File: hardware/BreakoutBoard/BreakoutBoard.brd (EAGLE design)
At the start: 90 x 56 mm, 38 parts, among them J1 CON-71741-2184-TOP, J10 CON-2X3-RASTER, J11 CON-2X3-RASTER, J12 CON-2X3-RASTER, J13 CON-2X4-RASTER, J2 CON-71741-2184-BOT, J3 CON-2X4-RASTER, J4 CON-2X10-RASTER, J5 CON-2X3-RASTER, J6 CON-2X3-RASTER, J7 CON-2X3-RASTER, J8 CON-2X3-RASTER, J9 CON-2X3-RASTER, M1 MOUNT-HOLE3.3, M2 MOUNT-HOLE3.3, M3 MOUNT-HOLE3.3, M4 MOUNT-HOLE3.3, M5 FIDUCIAL1X2, M6 FIDUCIAL1X2, M7 FIDUCIAL1X2, M8 FIDUCIAL1X2

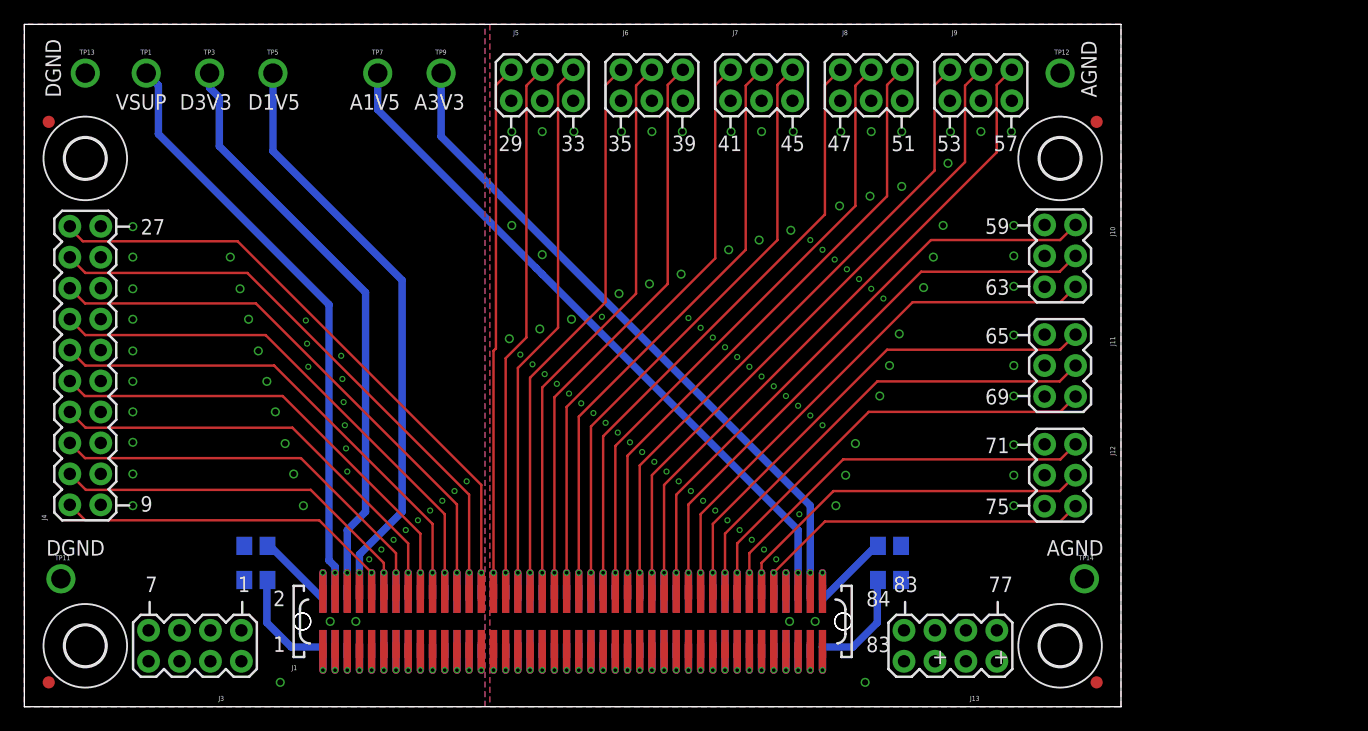
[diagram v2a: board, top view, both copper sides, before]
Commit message: - Ground planes changed - Supply wires
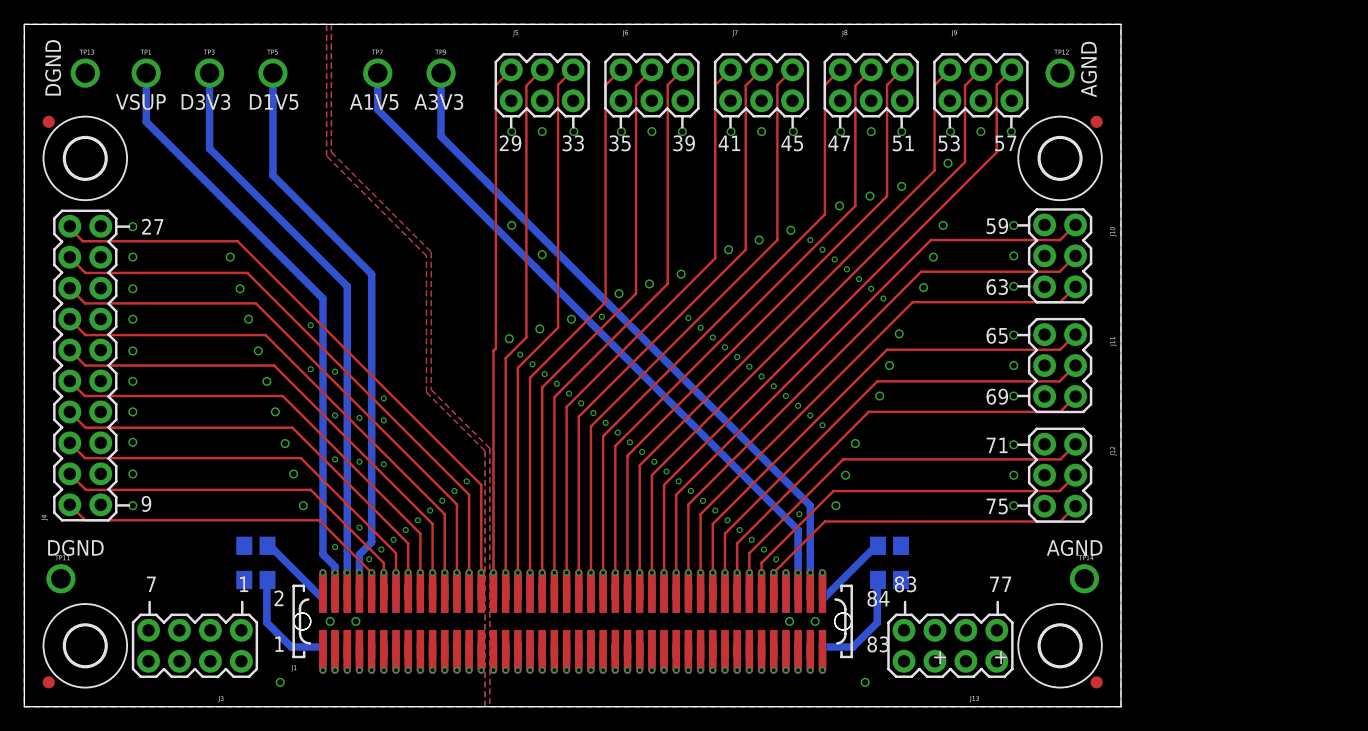
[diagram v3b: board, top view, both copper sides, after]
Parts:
- moved LOGO4 46.6 mm to (68.0, 15.0)
- moved LOGO1 45.9 mm to (12.0, 15.0)
- moved LOGO3 43.6 mm to (68.0, 25.5)
- moved LOGO2 32.9 mm to (12.0, 25.5)
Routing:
- net 8: track 76.5 -> 74.4 mm
- net 6: track 72.4 -> 71.2 mm
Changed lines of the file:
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@@
 <setting verticaltext="up"/>
 </settings>
-<grid distance="1" unitdist="mm" unit="mm" style="dots" multiple="1" display="yes" altdistance="0.1" altunitdist="mm" altunit="mm"/>
+<grid distance="1" unitdist="mm" unit="mm" style="dots" multiple="1" display="yes" altdistance="0.5" altunitdist="mm" altunit="mm"/>
 <layers>
-<layer number="1" name="Top" color="4" fill="1" visible="no" active="yes"/>
+<layer number="1" name="Top" color="4" fill="1" visible="yes" active="yes"/>
 <layer number="2" name="Even" color="2" fill="1" visible="no" active="yes"/>
-<layer number="3" name="Odd" color="4" fill="1" visible="yes" active="yes"/>
+<layer number="3" name="Odd" color="4" fill="1" visible="no" active="yes"/>
 <layer number="14" name="Route14" color="1" fill="6" visible="no" active="no"/>
 <layer number="15" name="Route15" color="4" fill="6" visible="no" active="no"/>
-<layer number="16" name="Bottom" color="1" fill="1" visible="yes" active="yes"/>
+<layer number="16" name="Bottom" color="1" fill="1" visible="no" active="yes"/>
 <layer number="17" name="Pads" color="2" fill="1" visible="yes" active="yes"/>
 <layer number="18" name="Vias" color="2" fill="1" visible="yes" active="yes"/>
@@
 <element name="M7" library="powerboard" package="FIDUCIAL-1X2" value="FIDUCIAL1X2" x="88" y="48"/>
 <element name="M8" library="powerboard" package="FIDUCIAL-1X2" value="FIDUCIAL1X2" x="88" y="2"/>
-<element name="LOGO1" library="Logo" package="LOGO-ISIS-10MM-GOLD" value="LOGO-ISIS-600MIL-10MM-AU" x="28" y="58"/>
-<element name="LOGO2" library="Logo" package="LOGO-VANDERBILT-10MM-GOLD" value="LOGO-VANDERBILT-600MIL-10MM-AU" x="17" y="58"/>
-<element name="LOGO3" library="Logo" package="LOGO-MARMOTE-10MM-GOLD" value="LOGO-MARMOTE-600MIL-10MM-AU" x="39" y="58"/>
-<element name="LOGO4" library="Logo" package="LOGO-MAGNIFYING-GLASS-10MM-GOLD" value="LOGO-MAGNIFYING-GLASS-600MIL-10MM-AU" x="50" y="58"/>
+<element name="LOGO1" library="Logo" package="LOGO-ISIS-10MM-GOLD" value="LOGO-ISIS-600MIL-10MM-AU" x="12" y="15"/>
+<element name="LOGO2" library="Logo" package="LOGO-VANDERBILT-10MM-GOLD" value="LOGO-VANDERBILT-600MIL-10MM-AU" x="12" y="25.5"/>
+<element name="LOGO3" library="Logo" package="LOGO-MARMOTE-10MM-GOLD" value="LOGO-MARMOTE-600MIL-10MM-AU" x="68" y="25.5"/>
+<element name="LOGO4" library="Logo" package="LOGO-MAGNIFYING-GLASS-10MM-GOLD" value="LOGO-MAGNIFYING-GLASS-600MIL-10MM-AU" x="68" y="15"/>
 <element name="TP1" library="BreakoutBoard" package="TESTPOINT" value="TESTPOINT-BLUE" x="10" y="52">
 <attribute name="DIGI-KEY#" value="5122K-ND" x="10" y="52" size="1.778" layer="27" display="off"/>
@@
 <vertex x="0" y="0"/>
 <vertex x="37.8" y="0"/>
-<vertex x="37.8" y="56"/>
+<vertex x="37.8" y="21"/>
+<vertex x="33" y="25.8"/>
+<vertex x="33" y="37"/>
+<vertex x="24.8" y="45.2"/>
+<vertex x="24.8" y="56"/>
 </polygon>
 <polygon width="0.2032" layer="16">
@@
 <vertex x="0" y="0"/>
 <vertex x="37.8" y="0"/>
-<vertex x="37.8" y="56"/>
+<vertex x="37.8" y="21"/>
+<vertex x="33" y="25.8"/>
+<vertex x="33" y="37"/>
+<vertex x="24.8" y="45.2"/>
+<vertex x="24.8" y="56"/>
 </polygon>
 <polygon width="0.2032" layer="3">
@@
 <vertex x="0" y="0"/>
 <vertex x="37.8" y="0"/>
-<vertex x="37.8" y="56"/>
+<vertex x="37.8" y="21"/>
+<vertex x="33" y="25.8"/>
+<vertex x="33" y="37"/>
+<vertex x="24.8" y="45.2"/>
+<vertex x="24.8" y="56"/>
 </polygon>
 <polygon width="0.2032" layer="2">
@@
 <vertex x="0" y="0"/>
 <vertex x="37.8" y="0"/>
-<vertex x="37.8" y="56"/>
+<vertex x="37.8" y="21"/>
+<vertex x="33" y="25.8"/>
+<vertex x="33" y="37"/>
+<vertex x="24.8" y="45.2"/>
+<vertex x="24.8" y="56"/>
 </polygon>
 <via x="8.9" y="16.5" extent="1-16" drill="0.5"/>
@@
 <via x="34.3" y="16.9" extent="1-16" drill="0.3048"/>
 <via x="35.3" y="17.7" extent="1-16" drill="0.3048"/>
-<via x="26.5" y="19.3" extent="1-16" drill="0.3048"/>
-<via x="26.4" y="21.2" extent="1-16" drill="0.3048"/>
-<via x="26.3" y="23.1" extent="1-16" drill="0.3048"/>
-<via x="26.2" y="25" extent="1-16" drill="0.3048"/>
-<via x="26.1" y="26.9" extent="1-16" drill="0.3048"/>
-<via x="26" y="28.8" extent="1-16" drill="0.3048"/>
-<via x="23.3" y="27.9" extent="1-16" drill="0.3048"/>
-<via x="23.2" y="29.8" extent="1-16" drill="0.3048"/>
-<via x="23.1" y="31.7" extent="1-16" drill="0.3048"/>
+<via x="27.5" y="20.1" extent="1-16" drill="0.3048"/>
+<via x="29.5" y="19.9" extent="1-16" drill="0.3048"/>
+<via x="25.5" y="23.9" extent="1-16" drill="0.3048"/>
+<via x="27.5" y="23.7" extent="1-16" drill="0.3048"/>
+<via x="29.5" y="23.5" extent="1-16" drill="0.3048"/>
+<via x="29.5" y="25.3" extent="1-16" drill="0.3048"/>
+<via x="23.5" y="27.7" extent="1-16" drill="0.3048"/>
+<via x="25.5" y="27.5" extent="1-16" drill="0.3048"/>
+<via x="23.5" y="31.3" extent="1-16" drill="0.3048"/>
 <via x="36.3" y="18.5" extent="1-16" drill="0.3048"/>
+<via x="25.5" y="20.3" extent="1-16" drill="0.3048"/>
+<via x="25.5" y="13.1" extent="1-16" drill="0.3048"/>
+<via x="27.5" y="14.7" extent="1-16" drill="0.3048"/>
 </signal>
 <signal name="1">
@@
 <wire x1="16.5" y1="2.5" x2="18.3" y2="2.5" width="0.2032" layer="2"/>
 <wire x1="19" y1="3.2" x2="18.3" y2="2.5" width="0.2032" layer="2"/>
-<wire x1="10" y1="52" x2="11" y2="51" width="0.6096" layer="16"/>
-<wire x1="11" y1="51" x2="11" y2="47" width="0.6096" layer="16"/>
-<wire x1="11" y1="47" x2="25" y2="33" width="0.6096" layer="16"/>
-<wire x1="25" y1="33" x2="25" y2="12" width="0.6096" layer="16"/>
-<wire x1="25" y1="12" x2="25.5" y2="11.5" width="0.6096" layer="16"/>
+<wire x1="10" y1="52" x2="10" y2="48" width="0.6096" layer="16"/>
+<wire x1="10" y1="48" x2="24.5" y2="33.5" width="0.6096" layer="16"/>
+<wire x1="24.5" y1="33.5" x2="24.5" y2="12.5" width="0.6096" layer="16"/>
+<wire x1="24.5" y1="12.5" x2="25.5" y2="11.5" width="0.6096" layer="16"/>
 <wire x1="25.5" y1="11.5" x2="25.5" y2="11" width="0.6096" layer="16"/>
 </signal>
@@
 <wire x1="14.56" y1="1.9" x2="18.7" y2="1.9" width="0.2032" layer="2"/>
 <wire x1="19.7" y1="2.9" x2="18.7" y2="1.9" width="0.2032" layer="2"/>
-<wire x1="26.5" y1="11" x2="26.5" y2="14.5" width="0.6096" layer="16"/>
-<wire x1="26.5" y1="14.5" x2="28" y2="16" width="0.6096" layer="16"/>
-<wire x1="28" y1="16" x2="28" y2="34" width="0.6096" layer="16"/>
-<wire x1="28" y1="34" x2="16" y2="46" width="0.6096" layer="16"/>
-<wire x1="16" y1="46" x2="16" y2="50" width="0.6096" layer="16"/>
-<wire x1="16" y1="50" x2="15.2" y2="50.8" width="0.6096" layer="16"/>
-<wire x1="15.2" y1="50.8" x2="15.2" y2="52" width="0.6096" layer="16"/>
+<wire x1="26.5" y1="11" x2="26.5" y2="34.5" width="0.6096" layer="16"/>
+<wire x1="26.5" y1="34.5" x2="15.2" y2="45.8" width="0.6096" layer="16"/>
+<wire x1="15.2" y1="45.8" x2="15.2" y2="52" width="0.6096" layer="16"/>
 </signal>
 <signal name="8">
@@
 <wire x1="20.4" y1="2.6" x2="19.1" y2="1.3" width="0.2032" layer="2"/>
 <wire x1="27.5" y1="11" x2="27.5" y2="12.5" width="0.6096" layer="16"/>
-<wire x1="27.5" y1="12.5" x2="31" y2="16" width="0.6096" layer="16"/>
-<wire x1="31" y1="16" x2="31" y2="35" width="0.6096" layer="16"/>
-<wire x1="31" y1="35" x2="20.4" y2="45.6" width="0.6096" layer="16"/>
-<wire x1="20.4" y1="45.6" x2="20.4" y2="52" width="0.6096" layer="16"/>
+<wire x1="27.5" y1="12.5" x2="28.5" y2="13.5" width="0.6096" layer="16"/>
+<wire x1="28.5" y1="13.5" x2="28.5" y2="35.5" width="0.6096" layer="16"/>
+<wire x1="28.5" y1="35.5" x2="20.4" y2="43.6" width="0.6096" layer="16"/>
+<wire x1="20.4" y1="43.6" x2="20.4" y2="52" width="0.6096" layer="16"/>
 </signal>
 <signal name="10">
@@
 <vertex x="90" y="0"/>
 <vertex x="90" y="56"/>
-<vertex x="38.2" y="56"/>
+<vertex x="25.2" y="56"/>
+<vertex x="25.2" y="45.5"/>
+<vertex x="33.4" y="37.3"/>
+<vertex x="33.4" y="26"/>
+<vertex x="38.2" y="21.2"/>
 </polygon>
 <polygon width="0.2032" layer="16">
@@
 <vertex x="90" y="0"/>
 <vertex x="90" y="56"/>
-<vertex x="38.2" y="56"/>
+<vertex x="25.2" y="56"/>
+<vertex x="25.2" y="45.5"/>
+<vertex x="33.4" y="37.3"/>
+<vertex x="33.4" y="26"/>
+<vertex x="38.2" y="21.2"/>
 </polygon>
 <polygon width="0.2032" layer="3">
@@
 <vertex x="90" y="0"/>
 <vertex x="90" y="56"/>
-<vertex x="38.2" y="56"/>
+<vertex x="25.2" y="56"/>
+<vertex x="25.2" y="45.5"/>
+<vertex x="33.4" y="37.3"/>
+<vertex x="33.4" y="26"/>
+<vertex x="38.2" y="21.2"/>
 </polygon>
 <polygon width="0.2032" layer="2">
@@
 <vertex x="90" y="0"/>
 <vertex x="90" y="56"/>
-<vertex x="38.2" y="56"/>
+<vertex x="25.2" y="56"/>
+<vertex x="25.2" y="45.5"/>
+<vertex x="33.4" y="37.3"/>
+<vertex x="33.4" y="26"/>
+<vertex x="38.2" y="21.2"/>
 </polygon>
 <via x="81.2" y="16.5" extent="1-16" drill="0.5"/>

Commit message: - Texts moved closer to edge, so they stay visible even if the board is covered
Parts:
- moved TP11 2.00 mm to (5.00, 10.5)
- moved TP14 2.00 mm to (85.0, 10.5)
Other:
- board text removed: "+"
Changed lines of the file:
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@@
 <layers>
 <layer number="1" name="Top" color="4" fill="1" visible="yes" active="yes"/>
-<layer number="2" name="Even" color="2" fill="1" visible="no" active="yes"/>
-<layer number="3" name="Odd" color="4" fill="1" visible="no" active="yes"/>
+<layer number="2" name="Even" color="2" fill="1" visible="yes" active="yes"/>
+<layer number="3" name="Odd" color="4" fill="1" visible="yes" active="yes"/>
 <layer number="14" name="Route14" color="1" fill="6" visible="no" active="no"/>
 <layer number="15" name="Route15" color="4" fill="6" visible="no" active="no"/>
-<layer number="16" name="Bottom" color="1" fill="1" visible="no" active="yes"/>
+<layer number="16" name="Bottom" color="1" fill="1" visible="yes" active="yes"/>
 <layer number="17" name="Pads" color="2" fill="1" visible="yes" active="yes"/>
 <layer number="18" name="Vias" color="2" fill="1" visible="yes" active="yes"/>
@@
 <text x="3" y="50" size="1.27" layer="21" font="vector" rot="R90">DGND</text>
 <text x="88" y="50" size="1.27" layer="21" font="vector" rot="R90">AGND</text>
-<text x="1.8" y="12.4" size="1.27" layer="21" font="vector">DGND</text>
-<text x="83.9" y="12.4" size="1.27" layer="21" font="vector">AGND</text>
-<text x="26.7" y="49" size="1.27" layer="21" font="vector">A1V5</text>
-<text x="32" y="49" size="1.27" layer="21" font="vector">A3V3</text>
-<text x="12.75" y="49" size="1.27" layer="21" font="vector">D3V3</text>
-<text x="18.35" y="49" size="1.27" layer="21" font="vector">D1V5</text>
-<text x="7.5" y="49" size="1.27" layer="21" font="vector">VSUP</text>
-<text x="74.5" y="3.5" size="1.27" layer="21" font="vector">+</text>
-<text x="79.5" y="3.5" size="1.27" layer="21" font="vector">+</text>
+<text x="3" y="8.3" size="1.27" layer="21" font="vector" rot="R90">DGND</text>
+<text x="88" y="8.4" size="1.27" layer="21" font="vector" rot="R90">AGND</text>
+<text x="26.7" y="54" size="1.27" layer="21" font="vector">A1V5</text>
+<text x="32" y="54" size="1.27" layer="21" font="vector">A3V3</text>
+<text x="12.75" y="54" size="1.27" layer="21" font="vector">D3V3</text>
+<text x="18.35" y="54" size="1.27" layer="21" font="vector">D1V5</text>
+<text x="7.5" y="54" size="1.27" layer="21" font="vector">VSUP</text>
 <wire x1="39.95" y1="47.55" x2="39.95" y2="48.45" width="0.2032" layer="21"/>
 <wire x1="45.05" y1="47.55" x2="45.05" y2="48.45" width="0.2032" layer="21"/>
@@
 <attribute name="MPN" value="5121" x="31.2" y="65" size="1.778" layer="27" display="off"/>
 </element>
-<element name="TP11" library="BreakoutBoard" package="TESTPOINT" value="TESTPOINT-YELLOW" x="3" y="10.5">
-<attribute name="DIGI-KEY#" value="5009K-ND" x="3" y="10.5" size="1.778" layer="27" display="off"/>
-<attribute name="MF" value="Keystone" x="3" y="10.5" size="1.778" layer="27" display="off"/>
-<attribute name="MPN" value="5009" x="3" y="10.5" size="1.778" layer="27" display="off"/>
-</element>
-<element name="TP14" library="BreakoutBoard" package="TESTPOINT" value="TESTPOINT-YELLOW" x="87" y="10.5">
-<attribute name="DIGI-KEY#" value="5009K-ND" x="87" y="10.5" size="1.778" layer="27" display="off"/>
-<attribute name="MF" value="Keystone" x="87" y="10.5" size="1.778" layer="27" display="off"/>
-<attribute name="MPN" value="5009" x="87" y="10.5" size="1.778" layer="27" display="off"/>
+<element name="TP11" library="BreakoutBoard" package="TESTPOINT" value="TESTPOINT-YELLOW" x="5" y="10.5">
+<attribute name="DIGI-KEY#" value="5009K-ND" x="5" y="10.5" size="1.778" layer="27" display="off"/>
+<attribute name="MF" value="Keystone" x="5" y="10.5" size="1.778" layer="27" display="off"/>
+<attribute name="MPN" value="5009" x="5" y="10.5" size="1.778" layer="27" display="off"/>
+</element>
+<element name="TP14" library="BreakoutBoard" package="TESTPOINT" value="TESTPOINT-YELLOW" x="85" y="10.5">
+<attribute name="DIGI-KEY#" value="5009K-ND" x="85" y="10.5" size="1.778" layer="27" display="off"/>
+<attribute name="MF" value="Keystone" x="85" y="10.5" size="1.778" layer="27" display="off"/>
+<attribute name="MPN" value="5009" x="85" y="10.5" size="1.778" layer="27" display="off"/>
 </element>
 <element name="TP13" library="BreakoutBoard" package="TESTPOINT" value="TESTPOINT-YELLOW" x="5" y="52">
@@
 </signal>
 </signals>
+<errors>
+</errors>
 </board>
 </drawing>
